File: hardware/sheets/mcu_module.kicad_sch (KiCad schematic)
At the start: 13 parts, among them U401 MDBT53-P1M, Y401 32.768kHz 9pF

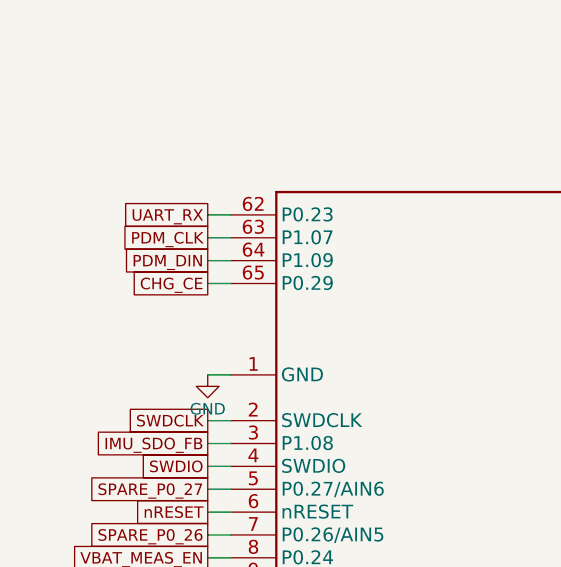
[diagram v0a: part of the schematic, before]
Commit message: hw: hold the charger CE high unless the MCU enables charging
CE was pulled up to 3V3, so with USB present and the logic rail absent
(the first milliseconds after attach, or a failed 3V3 rail) it went low
and the charger charged at its reset settings, whose cold limit can be
as low as -1.5 C.

R313 now pulls CE up to SYS, which is present whenever the battery or
USB is (CE is rated to 6 V). Q303 (AO3400A) pulls CE low only while
P0.29 drives the new CHG_EN net high, and R316 holds CHG_EN low
otherwise. Charging therefore stays off in MCU reset, with the MCU
unpowered or with 3V3 missing, not only at start-up.
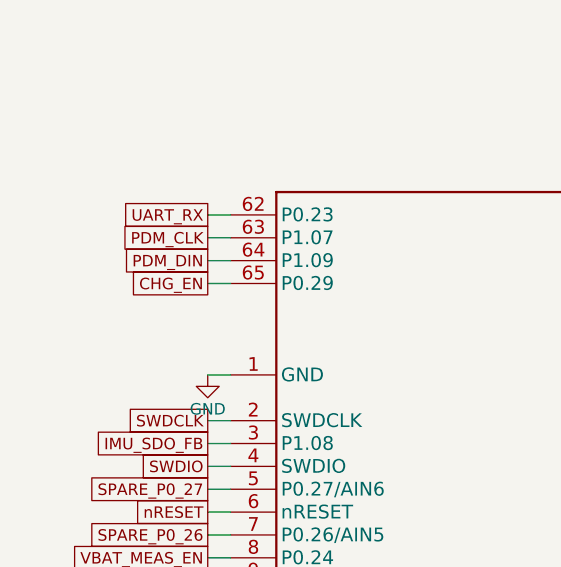
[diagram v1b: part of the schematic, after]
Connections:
- net CHG_CE renamed CHG_EN
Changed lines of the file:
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@@
 		)
 	)
-	(global_label "CHG_CE"
+	(global_label "CHG_EN"
 		(shape passive)
 		(at 109.22 73.66 180)

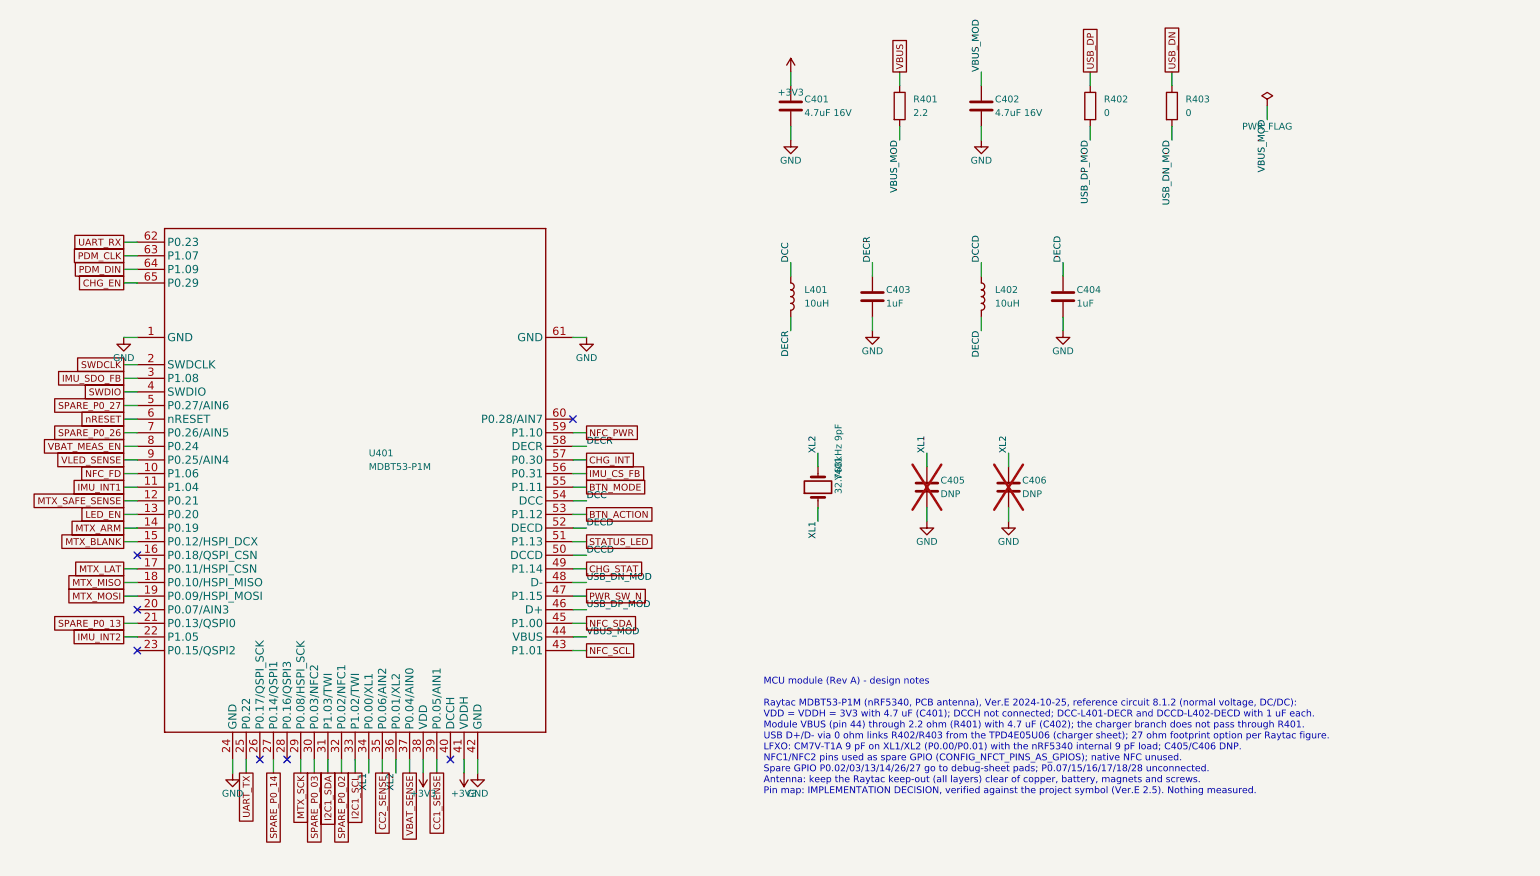
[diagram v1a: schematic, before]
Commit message: hw: switch U401 to the E73 nRF52840 module
The MDBT53-P1M cannot be sourced in time for the Rev A order, while
the E73-2G4M08S1C is stocked at JLCPCB (ADR 0015).

The E73 holds its DC/DC inductors and decoupling, so L401/L402 and
C403/C404 are removed. The nRF52840 has no internal 32.768 kHz load,
so C405/C406 are fitted with 12 pF; the value is calculated and still
needs checking against the Product Specification. All 29 module GPIO
are used: CHG_STAT is no longer read by the MCU, and the UART pads,
spare GPIO pads and IMU SPI-fallback links are removed. Pins Ebyte
marks as low-frequency carry only analog inputs or slow signals.
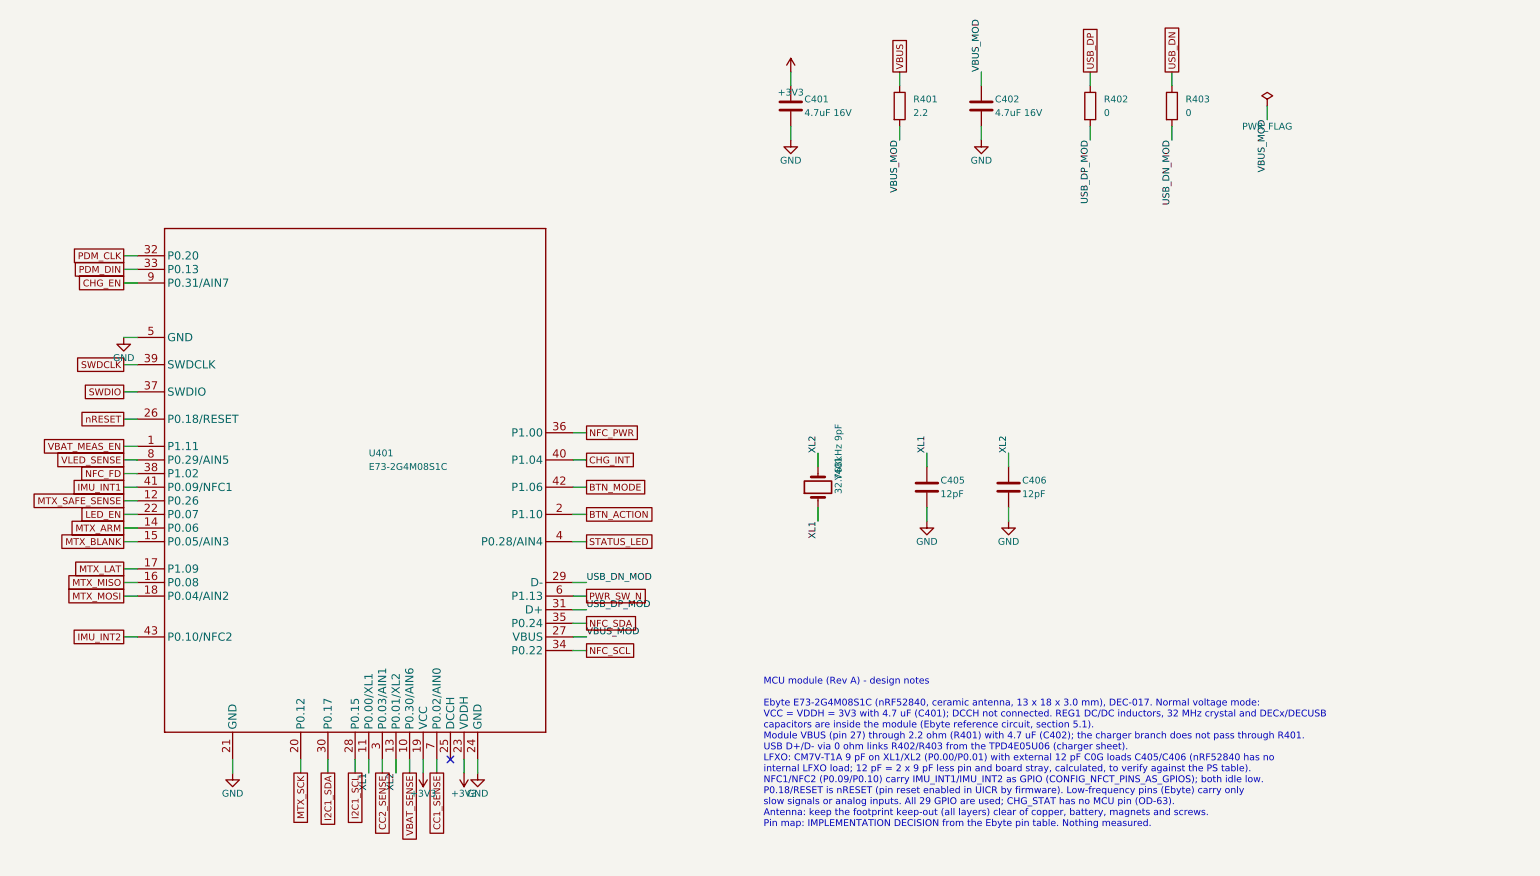
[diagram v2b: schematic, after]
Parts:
- removed C403, C404: 1uF, Capacitor_SMD:C_0402_1005Metric, symbol Device:C
- removed L401, L402: 10uH, Inductor_SMD:L_0603_1608Metric, symbol Device:L
- C405: value DNP -> 12pF; LCSC (none) -> C1547; MPN (none) -> 0402CG120J500NT; Manufacturer (none) -> FH; Note External XL1 load option (internal 9 pF used) -> nRF52840 LFXO load (external; 9 pF crystal), C0G; now fitted
- C406: value DNP -> 12pF; LCSC (none) -> C1547; MPN (none) -> 0402CG120J500NT; Manufacturer (none) -> FH; Note External XL2 load option (internal 9 pF used) -> nRF52840 LFXO load (external; 9 pF crystal), C0G; now fitted
- U401: value MDBT53-P1M -> E73-2G4M08S1C; footprint smart-led-badge:Raytac_MDBT53-P1M -> smart-led-badge:Ebyte_E73-2G4M08S1C; symbol smart-led-badge:MDBT53-P1M -> smart-led-badge:E73-2G4M08S1C; LCSC C5796572 -> C356849; MPN MDBT53-P1M -> E73-2G4M08S1C; Manufacturer Raytac -> Chengdu Ebyte Elec Tech; Note PCB antenna: keep-out per Raytac footprint rule area, every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 -> Ceramic antenna at the board edge: keep-out per footprint r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
- Y401: Note CL 9 pF, RS <= 70 kOhm; nRF5340 internal load set to 9 pF i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 -> CL 9 pF, RS <= 70 kOhm; external 12 pF loads C405/C406 (nRF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
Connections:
- net IMU_SDO_FB is gone; now on net CC2_SENSE: U401.3 (P0.03/AIN1)
- net SPARE_P0_02 is gone; now on net PDM_CLK: U401.32 (P0.20)
- net SPARE_P0_03 is gone; now on net I2C1_SDA: U401.30 (P0.17)
- net SPARE_P0_13 is gone; now on net GND: U401.21 (GND)
- net SPARE_P0_14 is gone; now on net VBUS_MOD: U401.27 (VBUS)
- net SPARE_P0_26 is gone; now on net CC1_SENSE: U401.7 (P0.02/AIN0)
- net SPARE_P0_27 is gone; now on net GND: U401.5 (GND)
- net +3V3: now also U401.19 (VCC), U401.23 (VDDH); no longer U401.38 (VDD), U401.41 (VDDH)
- net BTN_ACTION: now also U401.2 (P1.10); no longer U401.53 (P1.12)
- net BTN_MODE: now also U401.42 (P1.06); no longer U401.55 (P1.11)
- net CC1_SENSE: no longer U401.39 (P0.05/AIN1)
- net CC2_SENSE: no longer U401.35 (P0.06/AIN2)
- net CHG_EN: now also U401.9 (P0.31/AIN7); no longer U401.65 (P0.29)
- net CHG_INT: now also U401.40 (P1.04); no longer U401.57 (P0.30)
- net GND: no longer U401.1 (GND), U401.42 (GND), U401.61 (GND)
- net I2C1_SCL: now also U401.28 (P0.15); no longer U401.33 (P1.02/TWI)
- net I2C1_SDA: no longer U401.31 (P1.03/TWI)
- net IMU_INT1: now also U401.41 (P0.09/NFC1); no longer U401.11 (P1.04)
- net IMU_INT2: now also U401.43 (P0.10/NFC2); no longer U401.22 (P1.05)
- net LED_EN: now also U401.22 (P0.07); no longer U401.13 (P0.20)
- net MTX_MISO: now also U401.16 (P0.08); no longer U401.18 (P0.10/HSPI_MISO)
- net MTX_MOSI: now also U401.18 (P0.04/AIN2); no longer U401.19 (P0.09/HSPI_MOSI)
- net MTX_SCK: now also U401.20 (P0.12); no longer U401.29 (P0.08/HSPI_SCK)
- net NFC_FD: now also U401.38 (P1.02); no longer U401.10 (P1.06)
- net NFC_PWR: now also U401.36 (P1.00); no longer U401.59 (P1.10)
- net NFC_SCL: now also U401.34 (P0.22); no longer U401.43 (P1.01)
- net NFC_SDA: now also U401.35 (P0.24); no longer U401.45 (P1.00)
- net PDM_CLK: no longer U401.63 (P1.07)
- net PDM_DIN: now also U401.33 (P0.13); no longer U401.64 (P1.09)
- net PWR_SW_N: now also U401.6 (P1.13); no longer U401.47 (P1.15)
- net STATUS_LED: now also U401.4 (P0.28/AIN4); no longer U401.51 (P1.13)
- net SWDCLK: now also U401.39 (SWDCLK); no longer U401.2 (SWDCLK)
- net SWDIO: now also U401.37 (SWDIO); no longer U401.4 (SWDIO)
- net USB_DN_MOD: now also U401.29 (D-); no longer U401.48 (D-)
- net USB_DP_MOD: now also U401.31 (D+); no longer U401.46 (D+)
- net VBAT_MEAS_EN: now also U401.1 (P1.11); no longer U401.8 (P0.24)
- net VBAT_SENSE: now also U401.10 (P0.30/AIN6); no longer U401.37 (P0.04/AIN0)
- net VBUS_MOD: no longer U401.44 (VBUS)
- net VLED_SENSE: now also U401.8 (P0.29/AIN5); no longer U401.9 (P0.25/AIN4)
- net XL1: now also U401.11 (P0.00/XL1); no longer U401.34 (P0.00/XL1)
- net XL2: now also U401.13 (P0.01/XL2); no longer U401.36 (P0.01/XL2)
- net nRESET: now also U401.26 (P0.18/RESET); no longer U401.6 (nRESET)
- removed net CHG_STAT: U401.49 (P1.14)
- removed net DCC: U401.54 (DCC)
- removed net DCCD: U401.50 (DCCD)
- removed net DECD: U401.52 (DECD)
- removed net DECR: U401.58 (DECR)
- removed net IMU_CS_FB: U401.56 (P0.31)
- removed net UART_RX: U401.62 (P0.23)
- net UART_TX: no longer names the net of U401.25 (DCCH)
- no-connect marks 7 -> 1
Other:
- note added: "MCU module (Rev A) - design notes Ebyte E73-2G4M08S1C (nRF52840, ceramic antenna, 13 x 18 x 3.0 mm), DEC-017. Normal voltage mode: VCC = VDDH = 3V3 with 4.7 uF (C401); DCCH not connected. REG1 DC/DC inductors, 32 MHz crystal and DECx/DECUSB capacitors are inside the module (Ebyte reference circuit, section 5.1). Module VBUS (pin 27) through 2.2 ohm (R401) with 4.7 uF (C402); the charger branch do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"
- note removed: "MCU module (Rev A) - design notes Raytac MDBT53-P1M (nRF5340, PCB antenna), Ver.E 2024-10-25, reference circuit 8.1.2 (normal voltage, DC/DC): VDD = VDDH = 3V3 with 4.7 uF (C401); DCCH not connected; DCC-L401-DECR and DCCD-L402-DECD with 1 uF each. Module VBUS (pin 44) through 2.2 ohm (R401) with 4.7 uF (C402); the charger branch does not pass through R401. USB D+/D- via 0 ohm links R402/R403 fro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"
